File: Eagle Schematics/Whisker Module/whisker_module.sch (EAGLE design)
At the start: 72 parts, among them IC1 74LS14N, IC2 74LS14N, IC3 74LS14N, IC4 74LS14N, Q1 16MHZ, T1 BJT, T2 BJT, T3 BJT, T4 BJT

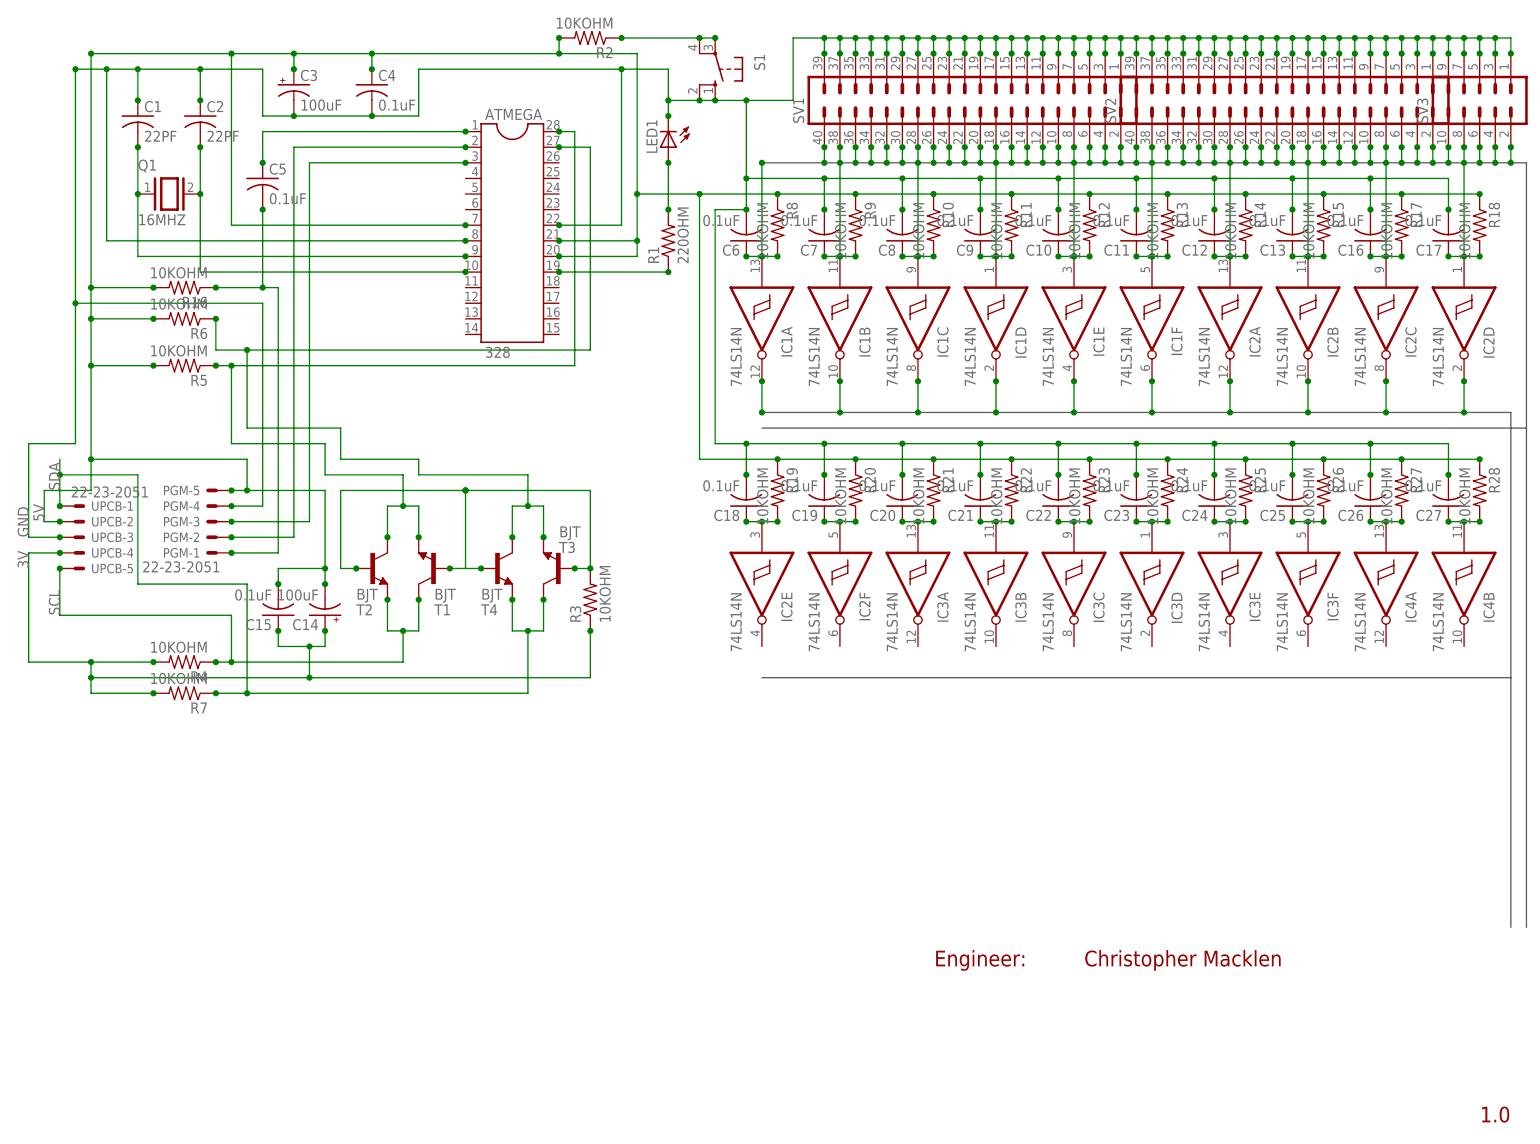
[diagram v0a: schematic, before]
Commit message: Finished both whisker modules
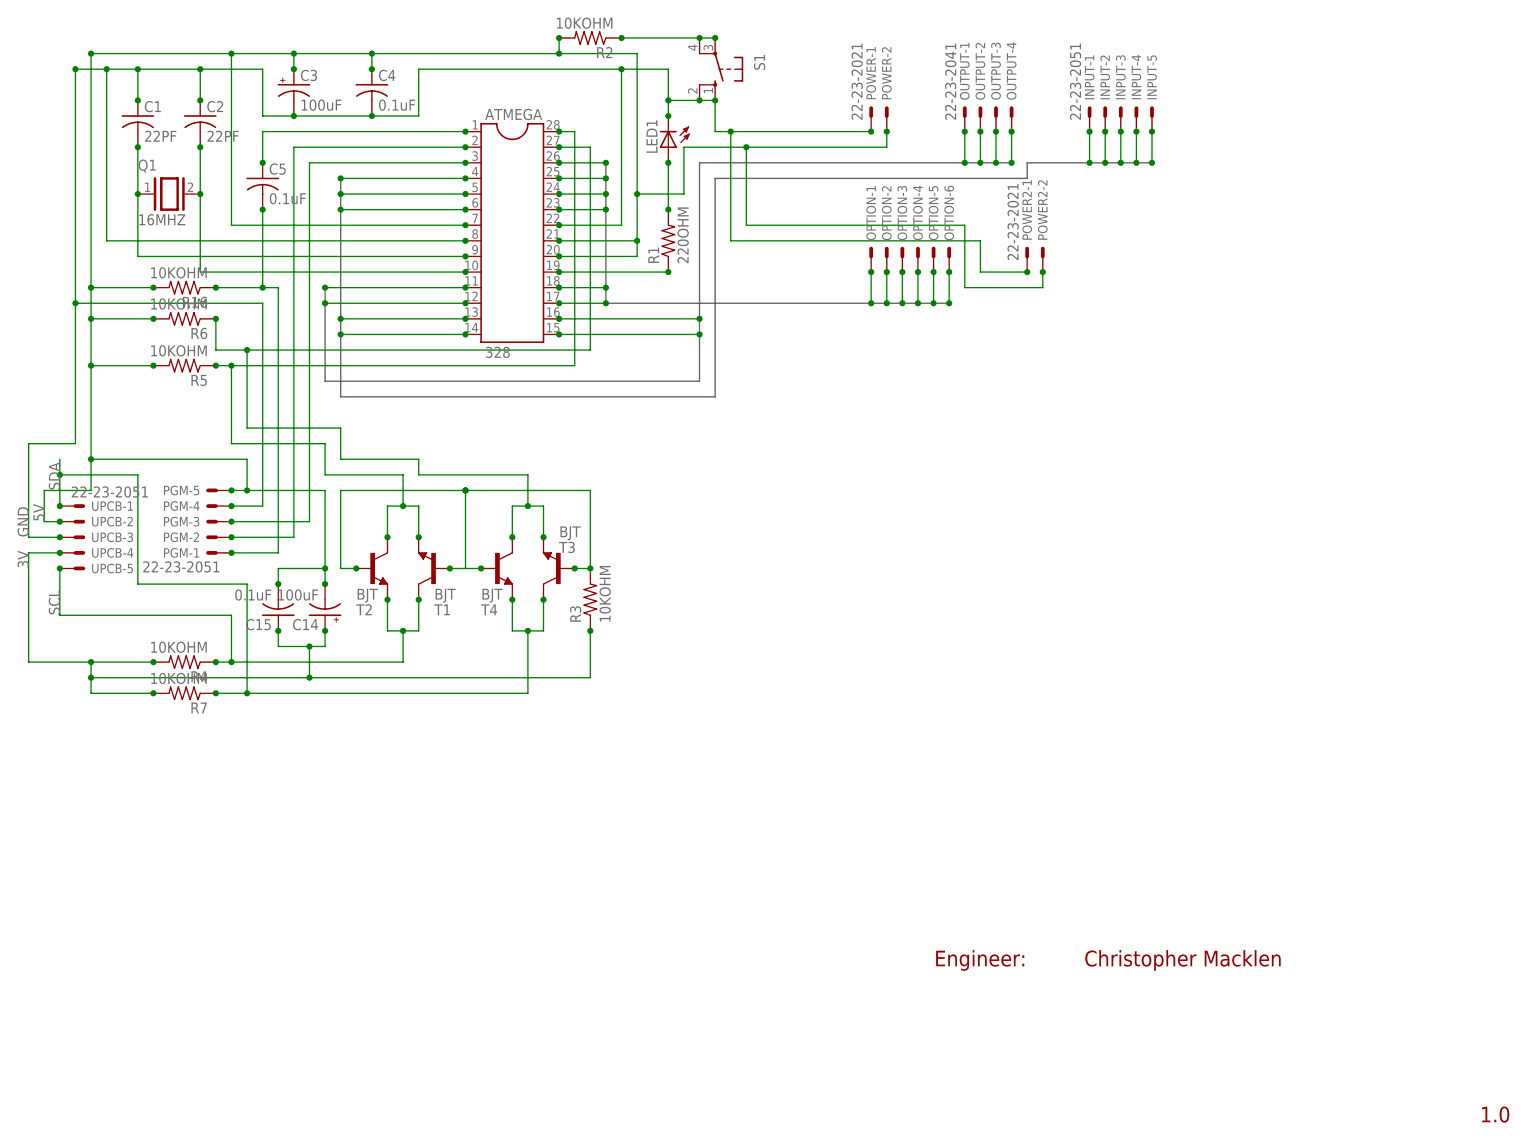
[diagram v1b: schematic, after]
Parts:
- removed C10, C11, C12, C13, C16, C17, C18, C19, C20, C21, C22, C23, C24, C25, C26, C27, C6, C7, C8, C9: 0.1uF, rcl:C-US025-024X044
- removed IC1, IC2, IC3, IC4: 74LS14N, 74xx-us:74LS14N
- removed R10, R11, R12, R13, R14, R15, R17, R18, R19, R20, R21, R22, R23, R24, R25, R26, R27, R28, R8, R9: 10KOHM, rcl:R-US_0204/7
- removed SV1, SV2: (no value), con-lstb:MA20-2W
- removed SV3: (no value), con-lstb:MA05-2
- added INPUT: 22-23-2051, con-molex:22-23-2051
- added OPTION: (no value), con-molex:22-23-2061
- added OUTPUT: 22-23-2041, con-molex:22-23-2041
- added POWER, POWER2: 22-23-2021, con-molex:22-23-2021
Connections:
- removed net D1: IC1A.O
- removed net D10: IC2D.O
- removed net D2: IC1B.O
- removed net D3: IC1C.O
- removed net D4: IC1D.O
- removed net D5: IC1E.O
- removed net D6: IC1F.O
- removed net D7: IC2A.O
- removed net D8: IC2B.O
- removed net D9: IC2C.O
- removed net W1: C6.1, IC1A.I, R8.2, SV1.40
- removed net W10: C17.1, IC2D.I, R18.2, SV1.22
- removed net W11: SV1.20
- removed net W12: SV1.18
- removed net W13: SV1.16
- removed net W14: SV1.14
- removed net W15: SV1.12
- removed net W16: SV1.10
- removed net W17: SV1.8
- removed net W18: SV1.6
- removed net W19: SV1.4
- removed net W2: C7.1, IC1B.I, R9.2, SV1.38
- removed net W20: SV1.2
- removed net W21: SV2.40
- removed net W22: SV2.38
- removed net W23: SV2.36
- removed net W24: SV2.34
- removed net W25: SV2.32
- removed net W26: SV2.30
- removed net W27: SV2.28
- removed net W28: SV2.26
- removed net W29: SV2.24
- removed net W3: C8.1, IC1C.I, R10.2, SV1.36
- removed net W30: SV2.22
- removed net W31: SV2.20
- removed net W32: SV2.18
- removed net W33: SV2.16
- removed net W34: SV2.14
- removed net W35: SV2.12
- removed net W36: SV2.10
- removed net W37: SV2.8
- removed net W38: SV2.6
- removed net W39: SV2.4
- removed net W4: C9.1, IC1D.I, R11.2, SV1.34
- removed net W40: SV2.2
- removed net W41: SV3.10
- removed net W42: SV3.8
- removed net W43: SV3.6
- removed net W44: SV3.4
- removed net W45: SV3.2
- removed net W46: C26.1, IC4A.I, R27.2
- removed net W47: C18.1, IC2E.I, R19.2
- removed net W48: C19.1, IC2F.I, R20.2
- removed net W49: C20.1, IC3A.I, R21.2
- removed net W5: C10.1, IC1E.I, R12.2, SV1.32
- removed net W50: C21.1, IC3B.I, R22.2
- removed net W51: C22.1, IC3C.I, R23.2
- removed net W52: C23.1, IC3D.I, R24.2
- removed net W53: C24.1, IC3E.I, R25.2
- removed net W54: C25.1, IC3F.I, R26.2
- removed net W55: C27.1, IC4B.I, R28.2
- removed net W6: C11.1, IC1F.I, R13.2, SV1.30
- removed net W7: C12.1, IC2A.I, R14.2, SV1.28
- removed net W8: C13.1, IC2B.I, R15.2, SV1.26
- removed net W9: C16.1, IC2C.I, R17.2, SV1.24
- new net IN1: ATMEGA.4, INPUT-1.S
- new net IN2: ATMEGA.5, INPUT-2.S
- new net IN3: ATMEGA.6, INPUT-3.S
- new net IN4: ATMEGA.13, INPUT-4.S
- new net IN5: ATMEGA.14, INPUT-5.S
- new net OPTION1: ATMEGA.26, OPTION-1.S
- new net OPTION2: ATMEGA.25, OPTION-2.S
- new net OPTION3: ATMEGA.24, OPTION-3.S
- new net OPTION4: ATMEGA.23, OPTION-4.S
- new net OPTION5: ATMEGA.18, OPTION-5.S
- new net OPTION6: ATMEGA.17, OPTION-6.S
- new net OUT1: ATMEGA.11, OUTPUT-1.S
- new net OUT2: ATMEGA.12, OUTPUT-2.S, OUTPUT-3.S
- new net OUT3: ATMEGA.15
- new net OUT4: ATMEGA.16, OUTPUT-4.S
- net 5V: now also POWER-2.S, POWER2-2.S; no longer R10.1, R11.1, R12.1, R13.1, R14.1, R15.1, R17.1, R18.1, R19.1, R20.1, R21.1, R22.1, R23.1, R24.1, R25.1, R26.1, R27.1, R28.1, R8.1, R9.1
- net GND: now also POWER-1.S, POWER2-1.S; no longer C10.2, C11.2, C12.2, C13.2, C16.2, C17.2, C18.2, C19.2, C20.2, C21.2, C22.2, C23.2, C24.2, C25.2, C26.2, C27.2, C6.2, C7.2, C8.2, C9.2, SV1.1, SV1.11, SV1.13, SV1.15, SV1.17, SV1.19, SV1.21, SV1.23, SV1.25, SV1.27, SV1.29, SV1.3, SV1.31, SV1.33, SV1.35, SV1.37, SV1.39, SV1.5, SV1.7, SV1.9, SV2.1, SV2.11, SV2.13, SV2.15, SV2.17, SV2.19, SV2.21, SV2.23, SV2.25, SV2.27, SV2.29, SV2.3, SV2.31, SV2.33, SV2.35, SV2.37, SV2.39, SV2.5, SV2.7, SV2.9, SV3.1, SV3.3, SV3.5, SV3.7, SV3.9

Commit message: Modified all schematics
Added a self debugging system.
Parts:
- removed INPUT: 22-23-2051, con-molex:22-23-2051
- removed OUTPUT: 22-23-2041, con-molex:22-23-2041
- removed POWER2: 22-23-2021, con-molex:22-23-2021
- added C10, C11, C12, C13, C16, C17, C18, C19, C20, C21, C22, C23, C24, C25, C26, C27, C28, C29, C30, C31, C32, C33, C34, C35, C36, C37, C38, C39, C40, C41, C42, C43, C44, C45, C46, C47, C6, C7, C8, C9: 0.1uF, rcl:C-US025-024X044
- added IC1, IC2, IC3, IC4, IC5, IC6, IC7: 74LS14N, 74xx-us:74LS14N
- added M1, M2, M3, M4, M5: CD74HCT151E, Custom:CD74HCT151E
- added POWER1, X1, X10, X11, X12, X13, X14, X15, X16, X17, X18, X19, X2, X20, X21, X22, X23, X24, X25, X26, X27, X28, X29, X3, X30, X31, X32, X33, X34, X35, X36, X37, X38, X39, X4, X40, X5, X6, X7, X8, X9: 22-23-2021, con-molex:22-23-2021
- added R10, R11, R12, R13, R14, R15, R17, R18, R19, R20, R21, R22, R23, R24, R25, R26, R27, R28, R29, R30, R31, R32, R33, R34, R35, R36, R37, R38, R39, R40, R41, R42, R43, R44, R45, R46, R47, R48, R8, R9: 10KOHM, rcl:R-US_0204/7
- added T10, T11, T12, T13, T14, T15, T16, T17, T18, T19, T20, T21, T22, T23, T24, T25, T26, T27, T28, T29, T30, T31, T32, T33, T34, T35, T36, T37, T38, T39, T40, T41, T42, T43, T44, T45, T6, T7, T8, T9: 2N3565, transistor:2N3565
- OPTION: value (none) -> 22-23-2051; device con-molex:22-23-2061 -> con-molex:22-23-2051
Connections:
- removed net IN1: ATMEGA.4, INPUT-1.S
- removed net IN2: ATMEGA.5, INPUT-2.S
- removed net IN3: ATMEGA.6, INPUT-3.S
- removed net IN4: ATMEGA.13, INPUT-4.S
- removed net IN5: ATMEGA.14, INPUT-5.S
- removed net OPTION6: ATMEGA.17, OPTION-6.S
- removed net OUT1: ATMEGA.11, OUTPUT-1.S
- removed net OUT2: ATMEGA.12, OUTPUT-2.S, OUTPUT-3.S
- removed net OUT3: ATMEGA.15
- removed net OUT4: ATMEGA.16, OUTPUT-4.S
- new net D1: IC1A.O, M1.I0
- new net D10: IC2D.O, M3.I1
- new net D11: IC2E.O, M1.I2
- new net D12: IC2F.O, M4.I2
- new net D13: IC3A.O, M2.I2
- new net D14: IC3B.O, M5.I2
- new net D15: IC3C.O, M3.I2
- new net D16: IC3D.O, M1.I3
- new net D17: IC3E.O, M4.I3
- new net D18: IC3F.O, M2.I3
- new net D19: IC4A.O, M5.I3
- new net D2: IC1B.O, M4.I0
- new net D20: IC4B.O, M3.I3
- new net D21: IC4C.O, M1.I4
- new net D22: IC4D.O, M4.I4
- new net D23: IC4E.O, M2.I4
- new net D24: IC4F.O, M5.I4
- new net D25: IC5A.O, M3.I4
- new net D26: IC5B.O, M1.I5
- new net D27: IC5C.O, M4.I5
- new net D28: IC5D.O, M2.I5
- new net D29: IC5E.O, M5.I5
- new net D3: IC1C.O, M2.I0
- new net D30: IC5F.O, M3.I5
- new net D31: IC6A.O, M1.I6
- new net D32: IC6B.O, M4.I6
- new net D33: IC6C.O, M2.I6
- new net D34: IC6D.O, M5.I6
- new net D35: IC6E.O, M3.I6
- new net D36: IC6F.O, M1.I7
- new net D37: IC7A.O, M4.I7
- new net D38: IC7B.O, M2.I7
- new net D39: IC7C.O, M5.I7
- new net D4: IC1D.O, M5.I0
- new net D40: IC7D.O, M3.I7
- new net D5: IC1E.O, M3.I0
- new net D6: IC1F.O, M1.I1
- new net D7: IC2A.O, M4.I1
- new net D8: IC2B.O, M2.I1
- new net D9: IC2C.O, M5.I1
- new net RESULT1: ATMEGA.4, M1.Y
- new net RESULT2: ATMEGA.5, M4.Y
- new net RESULT3: ATMEGA.6, M2.Y
- new net RESULT4: ATMEGA.13, M5.Y
- new net RESULT5: ATMEGA.14, M3.Y
- new net SELECT1: ATMEGA.11, M1.S0, M2.S0, M3.S0, M4.S0, M5.S0, M5.S1
- new net SELECT2: ATMEGA.12, M1.S1, M2.S1, M3.S1, M3.S2, M4.S1
- new net SELECT3: ATMEGA.15, M1.S2, M2.S2, M4.S2, M5.S2
- new net SELECT4: ATMEGA.16, M1.E', M1.GND, M2.E', M2.GND, M3.E', M3.GND, M4.E', M4.GND, M5.E', M5.GND
- new net SELECT5: ATMEGA.17, T10.B, T11.B, T12.B, T13.B, T14.B, T15.B, T16.B, T17.B, T18.B, T19.B, T20.B, T21.B, T22.B, T23.B, T24.B, T25.B, T26.B, T27.B, T28.B, T29.B, T30.B, T31.B, T32.B, T33.B, T34.B, T35.B, T36.B, T37.B, T38.B, T39.B, T40.B, T41.B, T42.B, T43.B, T44.B, T45.B, T6.B, T7.B, T8.B, T9.B
- new net W1: C6.1, IC1A.I, R8.2, T6.E, X40-2.S
- new net W10: C17.1, IC2D.I, R18.2, T15.E, X31-2.S
- new net W11: C18.1, IC2E.I, R19.2, T16.E, X30-2.S
- new net W12: C19.1, IC2F.I, R20.2, T17.E, X29-2.S
- new net W13: C20.1, IC3A.I, R21.2, T18.E, X28-2.S
- new net W14: C21.1, IC3B.I, R22.2, T19.E, X27-2.S
- new net W15: C22.1, IC3C.I, R23.2, T20.E, X26-2.S
- new net W16: C23.1, IC3D.I, R24.2, T21.E, X25-2.S
- new net W17: C24.1, IC3E.I, R25.2, T22.E, X24-2.S
- new net W18: C25.1, IC3F.I, R26.2, T23.E, X23-2.S
- new net W19: C26.1, IC4A.I, R27.2, T24.E, X22-2.S
- new net W2: C7.1, IC1B.I, R9.2, T7.E, X39-2.S
- new net W20: C27.1, IC4B.I, R28.2, T25.E, X21-2.S
- new net W21: C28.1, IC4C.I, R29.2, T26.E, X20-2.S
- new net W22: C29.1, IC4D.I, R30.2, T27.E, X19-2.S
- new net W23: C30.1, IC4E.I, R31.2, T28.E, X18-2.S
- new net W24: C31.1, IC4F.I, R32.2, T29.E, X17-2.S
- new net W25: C32.1, IC5A.I, R33.2, T30.E, X16-2.S
- new net W26: C33.1, IC5B.I, R34.2, T31.E, X15-2.S
- new net W27: C34.1, IC5C.I, R35.2, T32.E, X14-2.S
- new net W28: C35.1, IC5D.I, R36.2, T33.E, X13-2.S
- new net W29: C36.1, IC5E.I, R37.2, T34.E, X12-2.S
- new net W3: C8.1, IC1C.I, R10.2, T8.E, X38-2.S
- new net W30: C37.1, IC5F.I, R38.2, T35.E, X11-2.S
- new net W31: C38.1, IC6A.I, R39.2, T36.E, X10-2.S
- new net W32: C39.1, IC6B.I, R40.2, T37.E, X9-2.S
- new net W33: C40.1, IC6C.I, R41.2, T38.E, X8-2.S
- new net W34: C41.1, IC6D.I, R42.2, T39.E, X7-2.S
- new net W35: C42.1, IC6E.I, R43.2, T40.E, X6-2.S
- new net W36: C43.1, IC6F.I, R44.2, T41.E, X5-2.S
- new net W37: C44.1, IC7A.I, R45.2, T42.E, X4-2.S
- new net W38: C45.1, IC7B.I, R46.2, T43.E, X3-2.S
- new net W39: C46.1, IC7C.I, R47.2, T44.E, X2-2.S
- new net W4: C9.1, IC1D.I, R11.2, T9.E, X37-2.S
- new net W40: C47.1, IC7D.I, R48.2, T45.E, X1-2.S
- new net W5: C10.1, IC1E.I, R12.2, T10.E, X36-2.S
- new net W6: C11.1, IC1F.I, R13.2, T11.E, X35-2.S
- new net W7: C12.1, IC2A.I, R14.2, T12.E, X34-2.S
- new net W8: C13.1, IC2B.I, R15.2, T13.E, X33-2.S
- new net W9: C16.1, IC2C.I, R17.2, T14.E, X32-2.S
- net 5V: now also IC1P.VCC, IC2P.VCC, IC3P.VCC, IC4P.VCC, IC5P.VCC, IC6P.VCC, IC7P.VCC, M1.VCC, M2.VCC, M3.VCC, M4.VCC, M5.VCC, POWER1-2.S, R10.1, R11.1, R12.1, R13.1, R14.1, R15.1, R17.1, R18.1, R19.1, R20.1, R21.1, R22.1, R23.1, R24.1, R25.1, R26.1, R27.1, R28.1, R29.1, R30.1, R31.1, R32.1, R33.1, R34.1, R35.1, R36.1, R37.1, R38.1, R39.1, R40.1, R41.1, R42.1, R43.1, R44.1, R45.1, R46.1, R47.1, R48.1, R8.1, R9.1; no longer POWER2-2.S
- net GND: now also C10.2, C11.2, C12.2, C13.2, C16.2, C17.2, C18.2, C19.2, C20.2, C21.2, C22.2, C23.2, C24.2, C25.2, C26.2, C27.2, C28.2, C29.2, C30.2, C31.2, C32.2, C33.2, C34.2, C35.2, C36.2, C37.2, C38.2, C39.2, C40.2, C41.2, C42.2, C43.2, C44.2, C45.2, C46.2, C47.2, C6.2, C7.2, C8.2, C9.2, IC1P.GND, IC2P.GND, IC3P.GND, IC4P.GND, IC5P.GND, IC6P.GND, IC7P.GND, POWER1-1.S, T10.C, T11.C, T12.C, T13.C, T14.C, T15.C, T16.C, T17.C, T18.C, T19.C, T20.C, T21.C, T22.C, T23.C, T24.C, T25.C, T26.C, T27.C, T28.C, T29.C, T30.C, T31.C, T32.C, T33.C, T34.C, T35.C, T36.C, T37.C, T38.C, T39.C, T40.C, T41.C, T42.C, T43.C, T44.C, T45.C, T6.C, T7.C, T8.C, T9.C, X1-1.S, X10-1.S, X11-1.S, X12-1.S, X13-1.S, X14-1.S, X15-1.S, X16-1.S, X17-1.S, X18-1.S, X19-1.S, X2-1.S, X20-1.S, X21-1.S, X22-1.S, X23-1.S, X24-1.S, X25-1.S, X26-1.S, X27-1.S, X28-1.S, X29-1.S, X3-1.S, X30-1.S, X31-1.S, X32-1.S, X33-1.S, X34-1.S, X35-1.S, X36-1.S, X37-1.S, X38-1.S, X39-1.S, X4-1.S, X40-1.S, X5-1.S, X6-1.S, X7-1.S, X8-1.S, X9-1.S; no longer POWER2-1.S
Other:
- note added: "1"
- note added: "1.3"
- note added: "2"
- note added: "W1"
- note removed: "1.0"
